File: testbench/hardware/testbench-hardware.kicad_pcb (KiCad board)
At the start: 2 copper layers, 88.9 x 88.9 mm, 39 parts, among them J1 ZIF DIP-16 Socket, Q1 ZTX458, SW1 Action, SW2 Mode Select, SW3 Enable Power

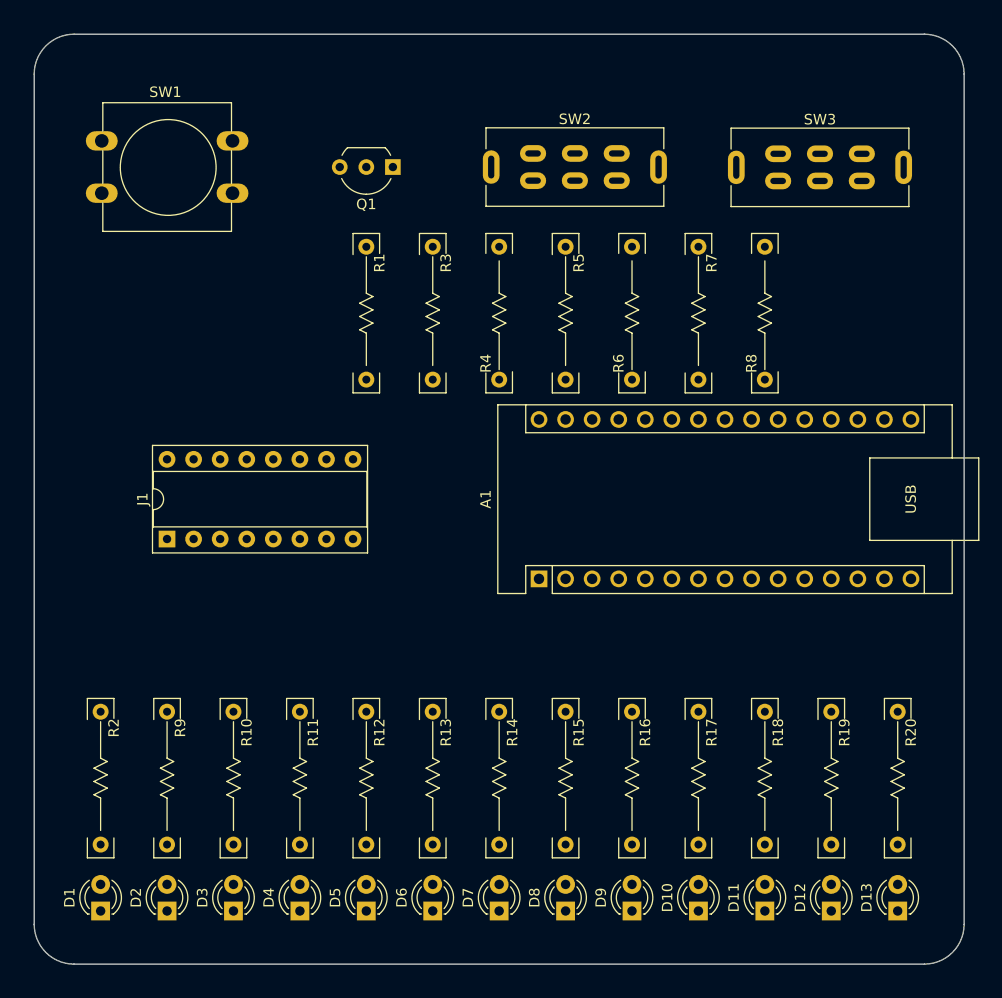
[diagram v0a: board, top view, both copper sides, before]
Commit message: [testbench] start wiring
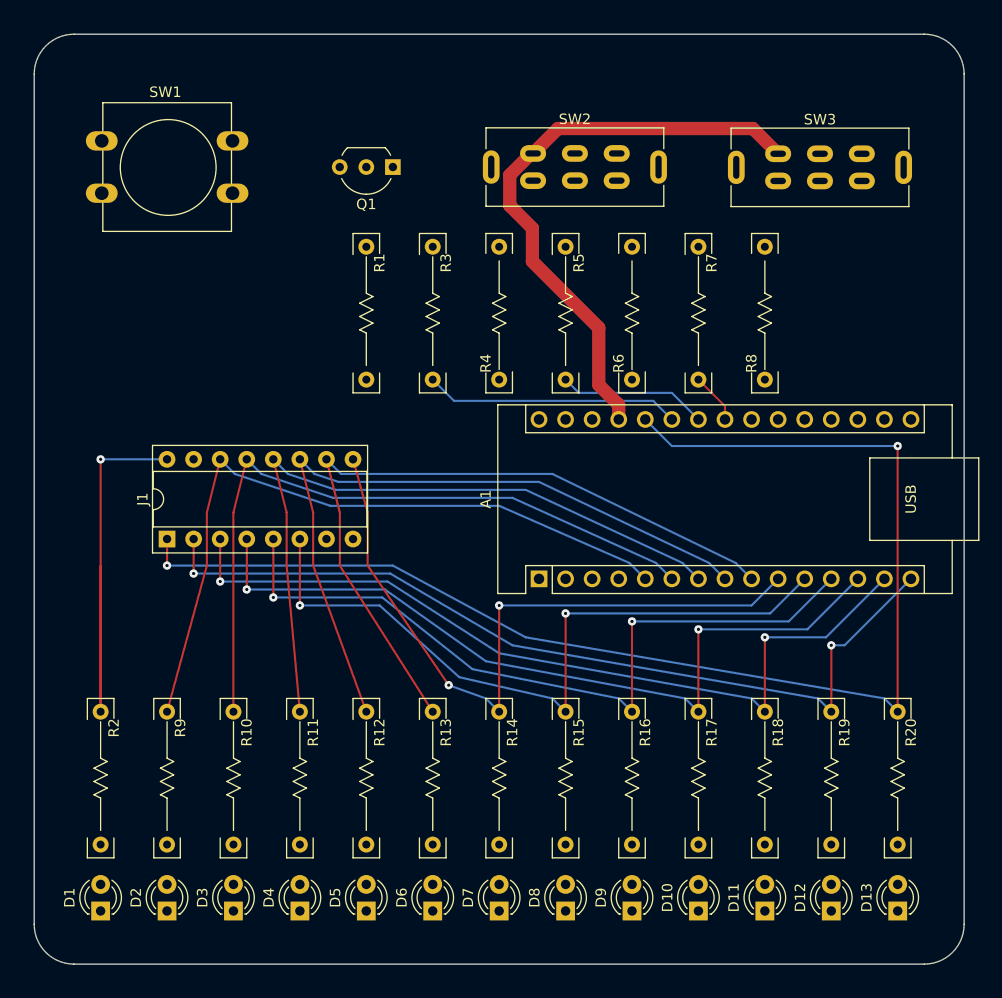
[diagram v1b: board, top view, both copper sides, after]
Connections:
- A1 pad 11: /R0 -> /B1
- A1 pad 12: /R1 -> /B0
- A1 pad 13: /V0 -> /V1
- A1 pad 14: /V1 -> /V0
- A1 pad 15: /B0 -> /R1
- A1 pad 18: Net-(A1-AREF) -> unconnected-(A1-AREF-Pad18)
- A1 pad 19: unconnected-(A1-A0-Pad19) -> Net-(A1-A0)
- A1 pad 26: /B1 -> /R0
- R1 pad 2: Net-(A1-AREF) -> Net-(A1-A0)
- R10 pad 1: /VERT -> /PASTEL
- R12 pad 1: /PASTEL -> /VERT
- R13 pad 1: /~{SUPPLT} -> /ROUGE
- R14 pad 1: /R0 -> /~{NOIR_INCR}
- R15 pad 1: /R1 -> /B1
- R16 pad 1: /V0 -> /B0
- R18 pad 1: /B0 -> /V0
- R19 pad 1: /B1 -> /R1
- R20 pad 1: /~{NOIR_INCR} -> /R0
- R9 pad 1: /ROUGE -> /~{SUPPLT}
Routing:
- net /R0: track 0.00 -> 125.7 mm, vias 0 -> 2
- net /R1: track 0.00 -> 83.7 mm, vias 0 -> 2
- net /V0: track 0.00 -> 79.9 mm, vias 0 -> 2
- net /V1: track 0.00 -> 76.2 mm, vias 0 -> 2
- net /B0: track 0.00 -> 72.4 mm, vias 0 -> 2
- net /ROUGE: track 0.00 -> 70.7 mm
- net /VERT: track 0.00 -> 68.9 mm
- net /B1: track 0.00 -> 68.8 mm, vias 0 -> 2
- net /~{SUPPLT}: track 0.00 -> 68.3 mm
- net /BLEU: track 0.00 -> 68.0 mm
- net /PASTEL: track 0.00 -> 67.9 mm
- net /~{NOIR_INCR}: track 0.00 -> 67.6 mm, vias 0 -> 2
- net +5V: track 0.00 -> 56.2 mm
- net /Vzif: track 0.00 -> 44.5 mm, vias 0 -> 1
- net Net-(A1-A6): track 0.00 -> 24.4 mm
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
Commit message: [testbench] done wiring
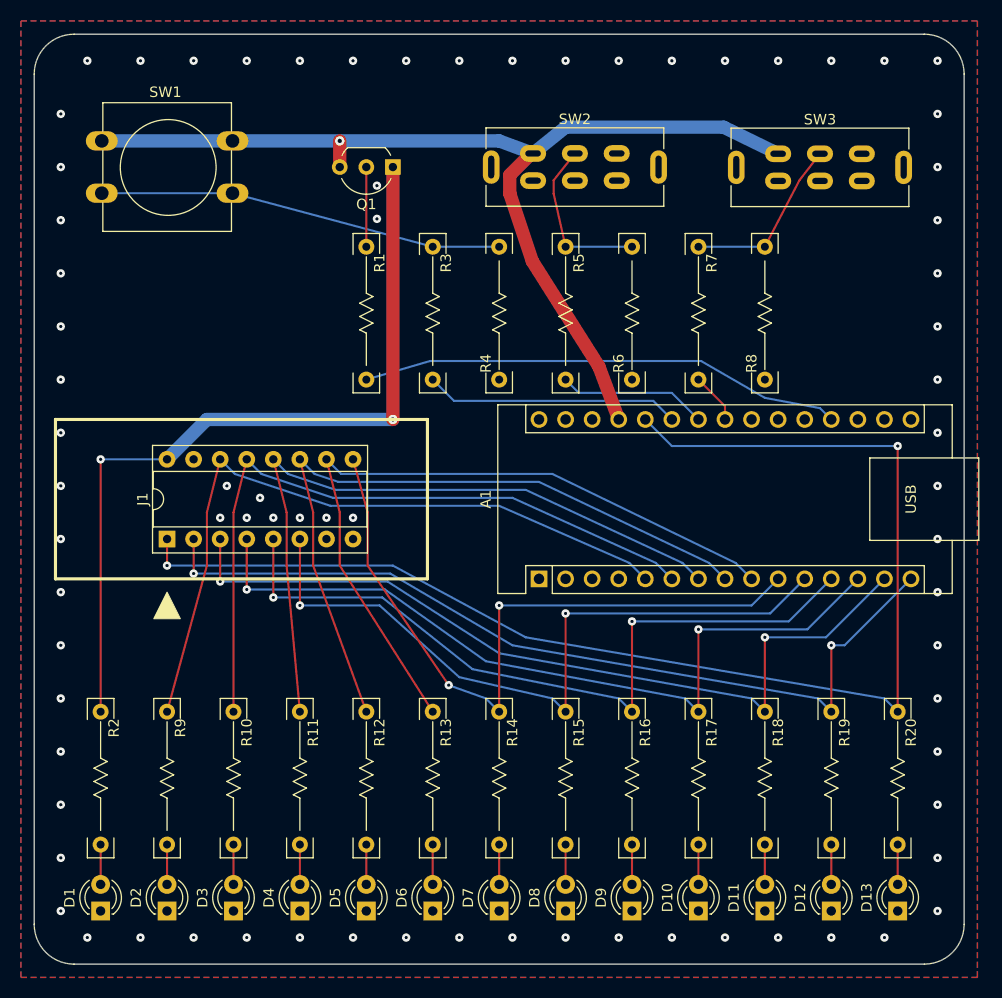
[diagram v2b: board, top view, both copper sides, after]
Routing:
- net Net-(A1-A0): track 0.00 -> 46.2 mm
- net +5V: track 56.2 -> 97.8 mm, vias 0 -> 1
- net Net-(R3-Pad1): track 0.00 -> 38.7 mm
- net /Vzif: track 44.5 -> 77.8 mm, vias 1 -> 2
- net Net-(SW3-B): track 0.00 -> 16.7 mm
- net Net-(SW2-B): track 0.00 -> 16.1 mm
- net Net-(Q1-B): track 0.00 -> 7.62 mm
- net Net-(D9-A): track 0.00 -> 3.81 mm
- net Net-(D8-A): track 0.00 -> 3.81 mm
- net Net-(D7-A): track 0.00 -> 3.81 mm
- net Net-(D6-A): track 0.00 -> 3.81 mm
- net Net-(D5-A): track 0.00 -> 3.81 mm
- net Net-(D4-A): track 0.00 -> 3.81 mm
- net Net-(D3-A): track 0.00 -> 3.81 mm
- net Net-(D2-A): track 0.00 -> 3.81 mm
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- added copper zone on B.Cu, net GND
- added copper zone on F.Cu, net GND

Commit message: [testbench] labels, cc-0 logos, tweak routing
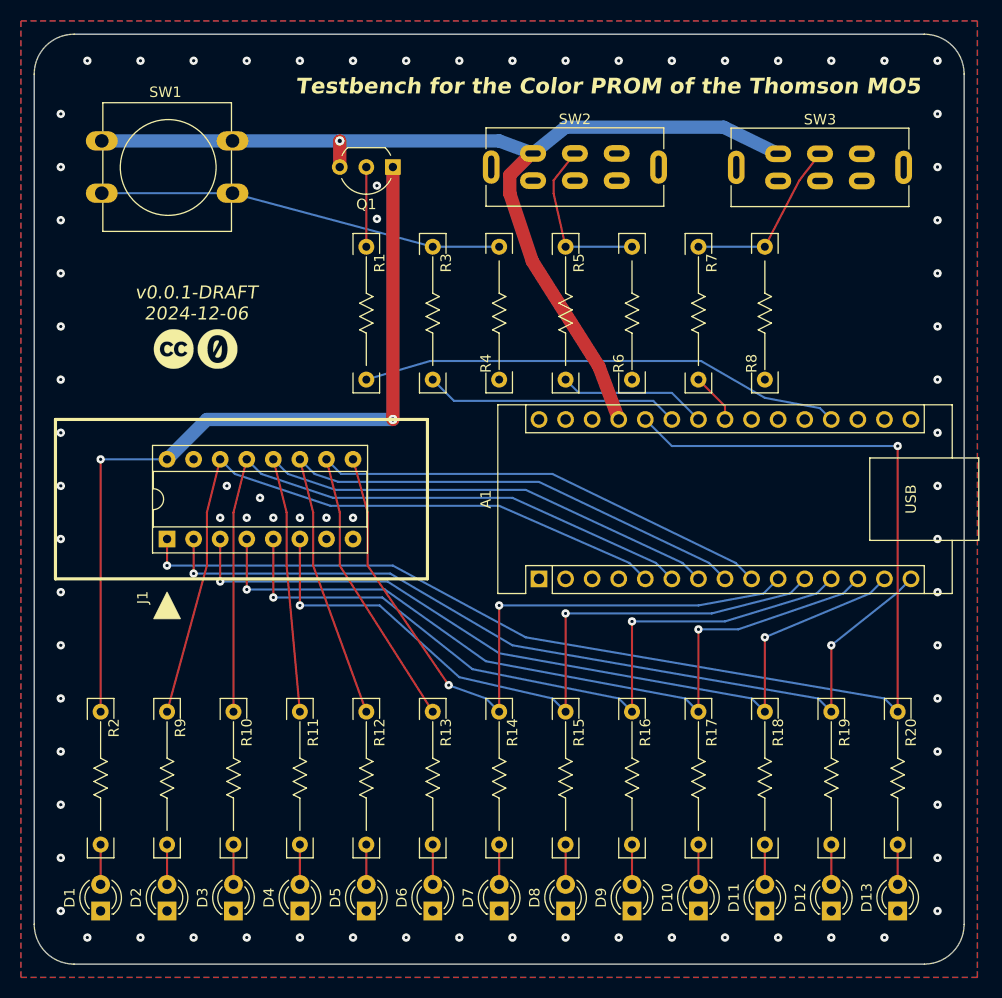
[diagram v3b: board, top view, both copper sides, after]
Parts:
- added G***: LOGO, cliparts:logo--cc--cc, F.Cu at (76.8, 93.6)
- added G***: LOGO, cliparts:logo--cc--zero, F.Cu at (81.0, 93.6)
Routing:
- net /V0: track 79.9 -> 79.0 mm
- net /V1: track 76.2 -> 75.3 mm
- net /B0: track 72.4 -> 71.7 mm
- net /B1: track 68.8 -> 68.2 mm
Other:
- board text added: "${REVISION} ${ISSUE_DATE}"
- board text added: "${TITLE}"

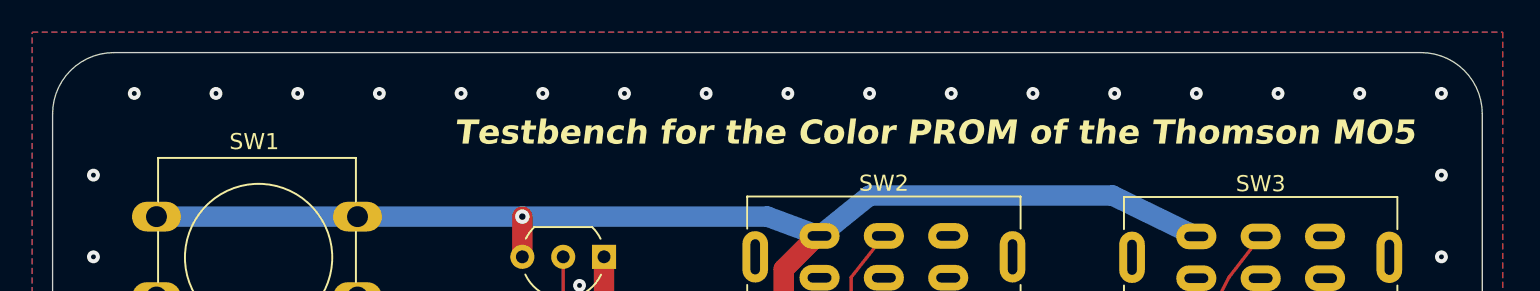
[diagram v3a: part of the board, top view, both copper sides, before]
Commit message: [testbench] mounting holes
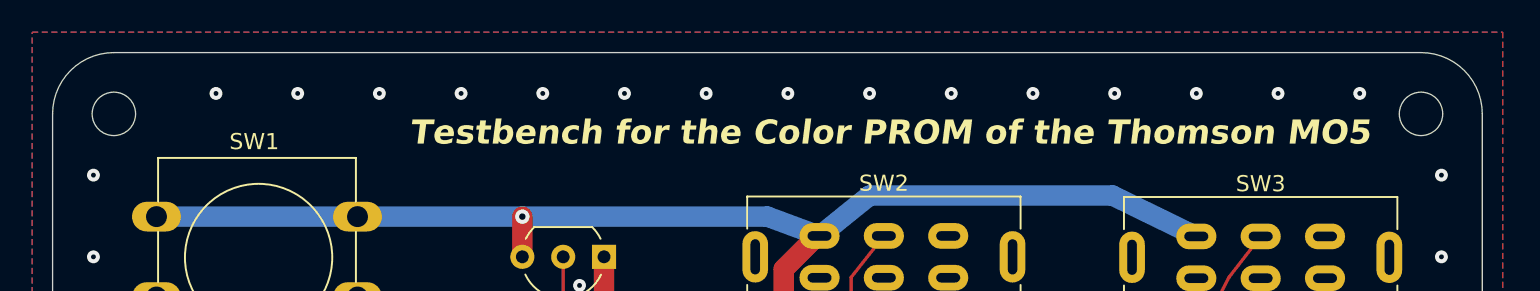
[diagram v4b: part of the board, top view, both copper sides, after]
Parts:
- added H1: M2.5, MountingHole:MountingHole_2.7mm_M2.5, F.Cu at (67.3, 67.3)
- added H2: M2.5, MountingHole:MountingHole_2.7mm_M2.5, F.Cu at (148.6, 67.3)
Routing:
- net GND: vias 75 -> 73
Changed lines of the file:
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@@
     )
+  )
+  (footprint "MountingHole:MountingHole_2.7mm_M2.5" (layer "F.Cu")
+    (at 148.59 67.31)
+    (descr "Mounting Hole 2.7mm, no annular, M2.5")
+    (tags "mounting hole 2.7mm no annular m2.5")
+    (property "Sheetfile" "testbench-hardware.kicad_sch")
+    (property "Sheetname" "")
+    (property "ki_description" "Mounting Hole without connection")
+    (property "ki_keywords" "mounting hole")
+    (attr exclude_from_pos_files)
+    (fp_text reference "H2" (at 0 -3.7) (layer "F.Fab")
+        (effects (font (size 1 1) (thickness 0.15)))
+    )
+    (fp_text value "M2.5" (at 0 3.7) (layer "F.Fab")
+        (effects (font (size 1 1) (thickness 0.15)))
+    )
+    (fp_text user "${REFERENCE}" (at 0 0) (layer "F.Fab")
+        (effects (font (size 1 1) (thickness 0.15)))
+    )
+    (fp_circle (center 0 0) (end 2.7 0)
+      (stroke (width 0.15) (type solid)) (fill none) (layer "Cmts.User"))
+    (fp_circle (center 0 0) (end 2.95 0)
+      (stroke (width 0.05) (type solid)) (fill none) (layer "F.CrtYd"))
+    (pad "" np_thru_hole circle (at 0 0) (size 2.7 2.7) (drill 2.7) (layers "*.Cu" "*.Mask"))
   )
   (footprint "commons-passives_THT:Passive_THT_resistor_W2.54mm_L12.70mm" (layer "F.Cu")
@@
       (rotate (xyz 0 0 0))
     )
+  )
+  (footprint "MountingHole:MountingHole_2.7mm_M2.5" (layer "F.Cu")
+    (at 67.31 67.31)
+    (descr "Mounting Hole 2.7mm, no annular, M2.5")
+    (tags "mounting hole 2.7mm no annular m2.5")
+    (property "Sheetfile" "testbench-hardware.kicad_sch")
+    (property "Sheetname" "")
+    (property "ki_description" "Mounting Hole without connection")
+    (property "ki_keywords" "mounting hole")
+    (attr exclude_from_pos_files)
+    (fp_text reference "H1" (at 0 -3.7) (layer "F.Fab")
+        (effects (font (size 1 1) (thickness 0.15)))
+    )
+    (fp_text value "M2.5" (at 0 3.7) (layer "F.Fab")
+        (effects (font (size 1 1) (thickness 0.15)))
+    )
+    (fp_text user "${REFERENCE}" (at 0 0) (layer "F.Fab")
+        (effects (font (size 1 1) (thickness 0.15)))
+    )
+    (fp_circle (center 0 0) (end 2.7 0)
+      (stroke (width 0.15) (type solid)) (fill none) (layer "Cmts.User"))
+    (fp_circle (center 0 0) (end 2.95 0)
+      (stroke (width 0.05) (type solid)) (fill none) (layer "F.CrtYd"))
+    (pad "" np_thru_hole circle (at 0 0) (size 2.7 2.7) (drill 2.7) (layers "*.Cu" "*.Mask"))
   )
   (footprint "LED_THT:LED_D3.0mm" (layer "F.Cu")
@@
   (gr_line (start 63.5 67.31) (end 67.31 67.31)
     (stroke (width 0.1) (type default)) (layer "User.2"))
-  (gr_text "${TITLE}" (at 118.364 69.342) (layer "F.SilkS")
+  (gr_text "${TITLE}" (at 115.57 69.342) (layer "F.SilkS")
     (effects (font (size 1.5 1.5) (thickness 0.3) bold italic) (justify bottom))
   )
@@
   (via (at 124.46 149.86) (size 0.8) (drill 0.3) (layers "F.Cu" "B.Cu") (free) (net 4))
   (via (at 81.28 109.728) (size 0.8) (drill 0.3) (layers "F.Cu" "B.Cu") (free) (net 4))
-  (via (at 149.86 66.04) (size 0.8) (drill 0.3) (layers "F.Cu" "B.Cu") (free) (net 4))
   (via (at 66.04 121.92) (size 0.8) (drill 0.3) (layers "F.Cu" "B.Cu") (free) (net 4))
   (via (at 104.14 149.86) (size 0.8) (drill 0.3) (layers "F.Cu" "B.Cu") (free) (net 4))
   (via (at 78.74 66.04) (size 0.8) (drill 0.3) (layers "F.Cu" "B.Cu") (free) (net 4))
   (via (at 66.04 147.32) (size 0.8) (drill 0.3) (layers "F.Cu" "B.Cu") (free) (net 4))
-  (via (at 68.58 66.04) (size 0.8) (drill 0.3) (layers "F.Cu" "B.Cu") (free) (net 4))
   (via (at 81.915 106.68) (size 0.8) (drill 0.3) (layers "F.Cu" "B.Cu") (free) (net 4))
   (via (at 83.82 66.04) (size 0.8) (drill 0.3) (layers "F.Cu" "B.Cu") (free) (net 4))
